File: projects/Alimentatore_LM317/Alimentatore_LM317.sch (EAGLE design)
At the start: 15 parts

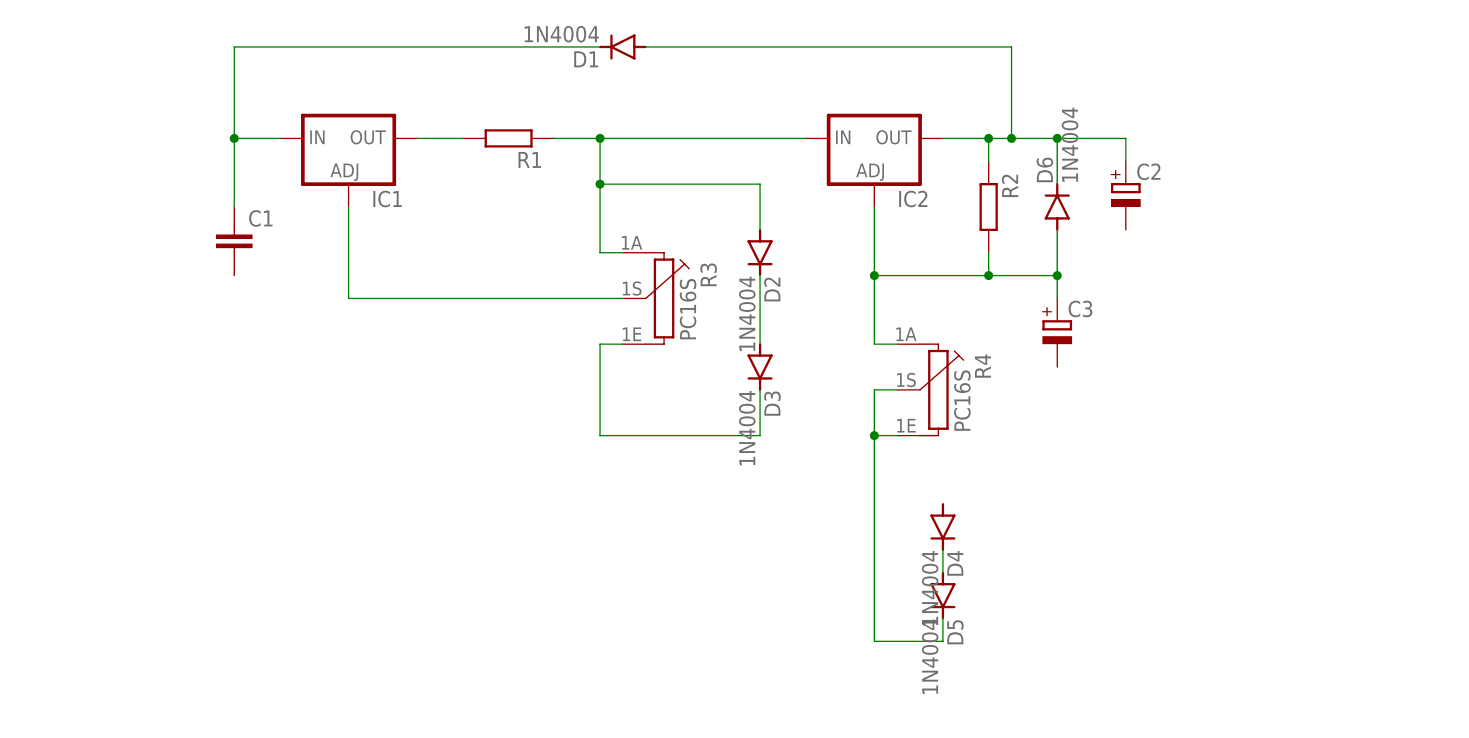
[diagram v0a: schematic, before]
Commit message: terminato primo schema alimentatore lm317
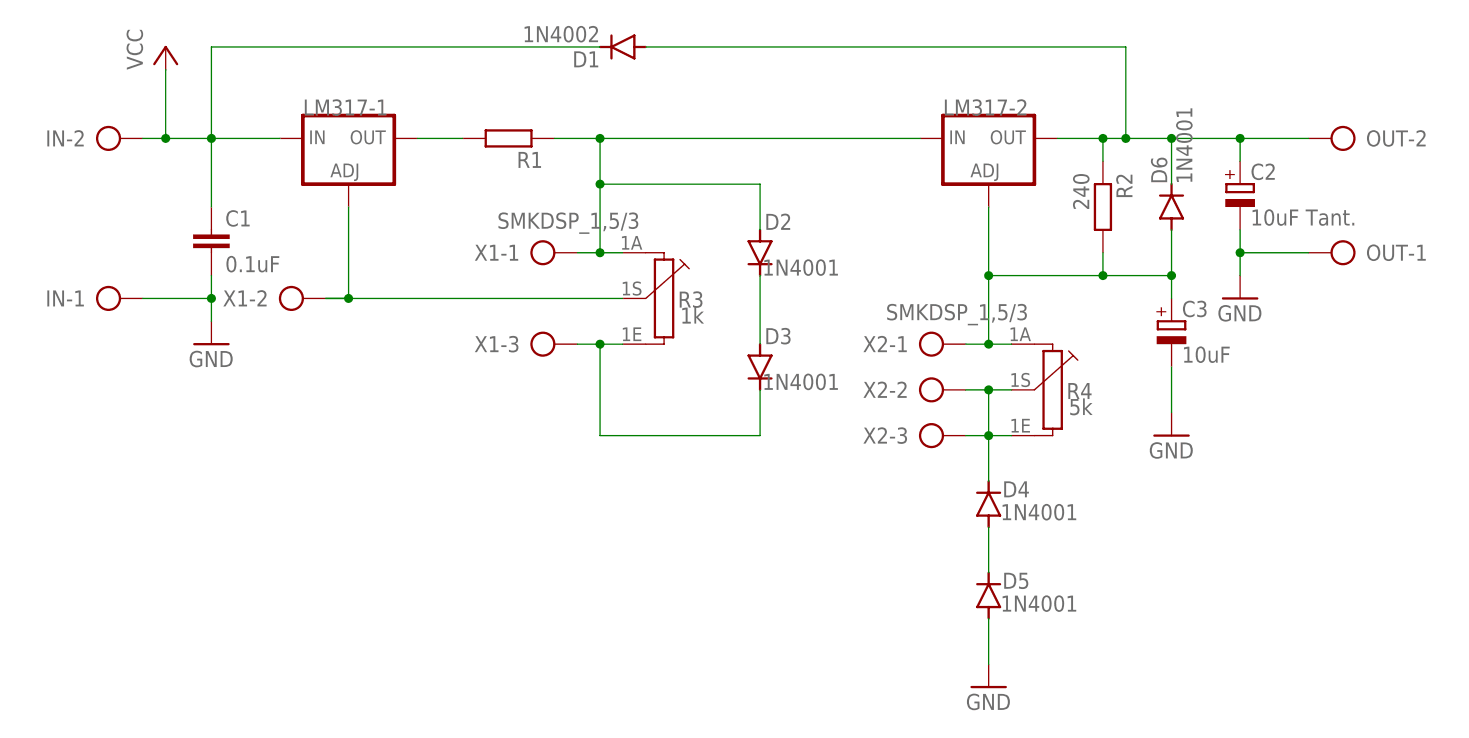
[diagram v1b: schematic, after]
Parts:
- removed IC1, IC2: (no value), v-reg:LM317TS
- added IN, OUT: SMKDSP_1,5/2, con-phoenix-smkdsp:SMKDSP_1,5/2
- added LM317-1, LM317-2: (no value), v-reg:LM317TS317TS_TO220
- added X1, X2: SMKDSP_1,5/3, con-phoenix-smkdsp:SMKDSP_1,5/3
- C1: value (none) -> 0.1uF
- C2: value (none) -> 10uF Tant.
- C3: value (none) -> 10uF
- D1: value 1N4004 -> 1N4002; device diode:1N4004 -> diode_MOD:1N4004DO-41
- D2, D3, D4, D5, D6: value 1N4004 -> 1N4001; device diode:1N4004 -> diode_MOD:1N4004DO-41
- R2: value (none) -> 240
- R3: value PC16S -> 1k
- R4: value PC16S -> 5k
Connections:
- removed net N$8: C2.+, D1.A, D6.C, IC2.OUT, R2.1
- new net GND: C1.2, C2.-, C3.-, D5.A, IN-1.KL, OUT-1.KL
- new net VCC: C1.1, D1.C, IN-2.KL, LM317-1.IN
- net N$1: now also C2.+, D1.A, D6.C, LM317-2.OUT, OUT-2.KL, R2.1; no longer C1.1, D1.C, IC1.IN
- net N$10: now also D4.C, X2-2.KL, X2-3.KL; no longer D5.C
- net N$2: now also LM317-1.OUT; no longer IC1.OUT
- net N$3: now also LM317-2.IN, X1-1.KL; no longer IC2.IN
- net N$5: now also LM317-1.ADJ, X1-2.KL; no longer IC1.ADJ
- net N$6: now also D4.A, D5.C; no longer D4.C, D5.A
- net N$7: now also X1-3.KL
- net N$9: now also LM317-2.ADJ, X2-1.KL; no longer IC2.ADJ
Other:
- moved on the sheet: C1, C2, C3, D4, D5, D6, R2, R4
